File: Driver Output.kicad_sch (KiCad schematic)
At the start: 13 parts, among them U1 DRV8300DRGER

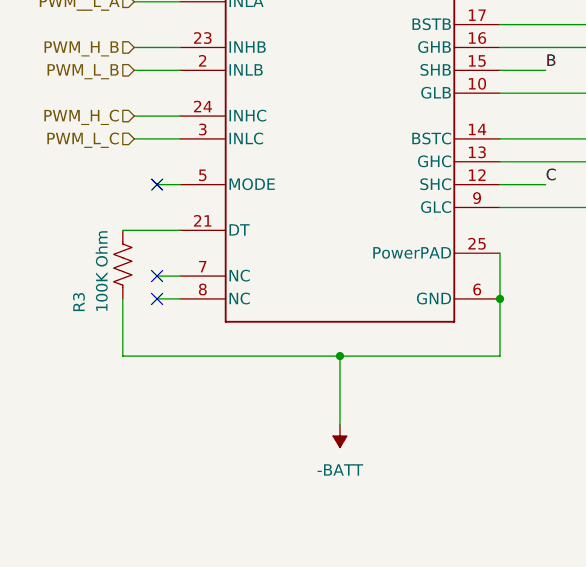
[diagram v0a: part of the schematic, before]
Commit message: Fixed pin names
reset pins to apply proper net names
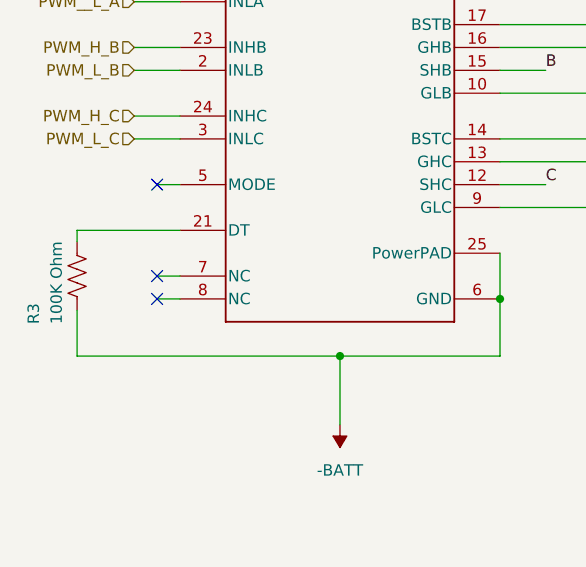
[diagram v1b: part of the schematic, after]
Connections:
- net -BATT: now reaches R10.1, R6.2, R8.1, R9.1
- net -BATT: now also C11.2, R3.2, U1.25 (PowerPAD), U1.6 (GND)
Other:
- moved on the sheet: R3

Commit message: more routing
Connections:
- net Half Bridge - 6S 50A - 2/BST_X renamed BSTB
- net Half Bridge - 6S 50A - 2/GATE_HIGH_X renamed GHB
- net Half Bridge - 6S 50A - 2/GATE_LOW_X renamed GLB
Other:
- sheet Half Bridge - 6S 50A - 1 ports: added X; removed none
- sheet Half Bridge - 6S 50A - 2 ports: added X; removed none
- sheet Half Bridge - 6S 50A - 3 ports: added X; removed none
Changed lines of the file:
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@@
 	(wire
 		(pts
-			(xy 83.82 90.17) (xy 95.25 90.17)
-		)
-		(stroke
-			(width 0)
-			(type default)
-		)
-	)
-	(wire
-		(pts
-			(xy 83.82 74.93) (xy 88.9 74.93)
+			(xy 83.82 90.17) (xy 135.89 90.17)
+		)
+		(stroke
+			(width 0)
+			(type default)
+		)
+	)
+	(wire
+		(pts
+			(xy 83.82 74.93) (xy 97.79 74.93)
 		)
 		(stroke
@@
 	(wire
 		(pts
+			(xy 83.82 59.69) (xy 135.89 59.69)
+		)
+		(stroke
+			(width 0)
+			(type default)
+		)
+	)
+	(wire
+		(pts
 			(xy 66.04 177.8) (xy 66.04 180.34)
 		)
@@
 	(wire
 		(pts
-			(xy 83.82 87.63) (xy 88.9 87.63)
-		)
-		(stroke
-			(width 0)
-			(type default)
-		)
-	)
-	(wire
-		(pts
-			(xy 95.25 62.23) (xy 97.79 62.23)
+			(xy 83.82 87.63) (xy 135.89 87.63)
 		)
 		(stroke
@@
 	(wire
 		(pts
-			(xy 96.52 74.93) (xy 97.79 74.93)
-		)
-		(stroke
-			(width 0)
-			(type default)
-		)
-	)
-	(wire
-		(pts
 			(xy 41.91 57.15) (xy 48.26 57.15)
 		)
@@
 	(wire
 		(pts
-			(xy 83.82 64.77) (xy 95.25 64.77)
+			(xy 83.82 64.77) (xy 135.89 64.77)
 		)
 		(stroke
@@
 	(wire
 		(pts
+			(xy 83.82 57.15) (xy 135.89 57.15)
+		)
+		(stroke
+			(width 0)
+			(type default)
+		)
+	)
+	(wire
+		(pts
 			(xy 60.96 152.4) (xy 80.01 152.4)
 		)
@@
 	(wire
 		(pts
-			(xy 96.52 77.47) (xy 96.52 74.93)
-		)
-		(stroke
-			(width 0)
-			(type default)
-		)
-	)
-	(wire
-		(pts
-			(xy 83.82 59.69) (xy 97.79 59.69)
-		)
-		(stroke
-			(width 0)
-			(type default)
-		)
-	)
-	(wire
-		(pts
 			(xy 50.8 163.83) (xy 55.88 163.83)
 		)
@@
 	(wire
 		(pts
-			(xy 83.82 85.09) (xy 97.79 85.09)
-		)
-		(stroke
-			(width 0)
-			(type default)
-		)
-	)
-	(wire
-		(pts
-			(xy 95.25 64.77) (xy 95.25 62.23)
-		)
-		(stroke
-			(width 0)
-			(type default)
-		)
-	)
-	(wire
-		(pts
-			(xy 83.82 62.23) (xy 88.9 62.23)
-		)
-		(stroke
-			(width 0)
-			(type default)
-		)
-	)
-	(wire
-		(pts
-			(xy 83.82 77.47) (xy 96.52 77.47)
+			(xy 83.82 85.09) (xy 135.89 85.09)
+		)
+		(stroke
+			(width 0)
+			(type default)
+		)
+	)
+	(wire
+		(pts
+			(xy 83.82 62.23) (xy 135.89 62.23)
+		)
+		(stroke
+			(width 0)
+			(type default)
+		)
+	)
+	(wire
+		(pts
+			(xy 83.82 77.47) (xy 97.79 77.47)
 		)
 		(stroke
@@
 	(wire
 		(pts
-			(xy 83.82 57.15) (xy 97.79 57.15)
-		)
-		(stroke
-			(width 0)
-			(type default)
-		)
-	)
-	(wire
-		(pts
 			(xy 36.83 101.6) (xy 36.83 106.68)
 		)
@@
 	(wire
 		(pts
-			(xy 95.25 87.63) (xy 97.79 87.63)
-		)
-		(stroke
-			(width 0)
-			(type default)
-		)
-	)
-	(wire
-		(pts
 			(xy 60.96 162.56) (xy 60.96 163.83)
 		)
@@
 	(wire
 		(pts
-			(xy 95.25 90.17) (xy 95.25 87.63)
-		)
-		(stroke
-			(width 0)
-			(type default)
-		)
-	)
-	(wire
-		(pts
-			(xy 83.82 82.55) (xy 97.79 82.55)
+			(xy 83.82 82.55) (xy 135.89 82.55)
 		)
 		(stroke
@@
 		)
 	)
+	(label "GHB"
+		(at 88.9 72.39 0)
+		(effects
+			(font
+				(size 1.27 1.27)
+			)
+			(justify left bottom)
+		)
+	)
+	(label "BSTB"
+		(at 88.9 69.85 0)
+		(effects
+			(font
+				(size 1.27 1.27)
+			)
+			(justify left bottom)
+		)
+	)
 	(label "A"
 		(at 88.9 62.23 180)
@@
 		)
 	)
+	(label "GLB"
+		(at 88.9 77.47 0)
+		(effects
+			(font
+				(size 1.27 1.27)
+			)
+			(justify left bottom)
+		)
+	)
+	(label "C"
+		(at 88.9 87.63 0)
+		(effects
+			(font
+				(size 1.27 1.27)
+			)
+			(justify left bottom)
+		)
+	)
 	(label "B"
 		(at 99.06 147.32 180)
@@
 			)
 			(justify right bottom)
-		)
-	)
-	(label "C"
-		(at 88.9 87.63 0)
-		(effects
-			(font
-				(size 1.27 1.27)
-			)
-			(justify left bottom)
 		)
 	)
@@
 	)
 	(sheet
-		(at 97.79 55.88)
-		(size 17.78 7.62)
+		(at 135.89 55.88)
+		(size 17.78 10.16)
 		(fields_autoplaced yes)
 		(stroke
@@
 		)
 		(property "Sheetname" "Half Bridge - 6S 50A - 1"
-			(at 97.79 55.1684 0)
+			(at 135.89 55.1684 0)
 			(effects
 				(font
@@
 		)
 		(property "Sheetfile" "Half Bridge - 6S 50A.kicad_sch"
-			(at 97.79 64.0846 0)
+			(at 135.89 66.6246 0)
 			(effects
 				(font
@@
 		)
 		(pin "BST_X" input
-			(at 97.79 57.15 180)
+			(at 135.89 57.15 180)
 			(effects
 				(font
@@
 		)
 		(pin "GATE_LOW_X" input
-			(at 97.79 62.23 180)
+			(at 135.89 64.77 180)
 			(effects
 				(font
@@
 		)
 		(pin "GATE_HIGH_X" input
-			(at 97.79 59.69 180)
+			(at 135.89 59.69 180)
+			(effects
+				(font
+					(size 1.27 1.27)
+				)
+				(justify left)
+			)
+		)
+		(pin "X" input
+			(at 135.89 62.23 180)
 			(effects
 				(font
@@
 	)
 	(sheet
-		(at 97.79 81.28)
-		(size 17.78 7.62)
+		(at 135.89 81.28)
+		(size 17.78 10.16)
 		(fields_autoplaced yes)
 		(stroke
@@
 		)
 		(property "Sheetname" "Half Bridge - 6S 50A - 3"
-			(at 97.79 80.5684 0)
+			(at 135.89 80.5684 0)
 			(effects
 				(font
@@
 		)
 		(property "Sheetfile" "Half Bridge - 6S 50A.kicad_sch"
-			(at 97.79 89.4846 0)
+			(at 135.89 92.0246 0)
 			(effects
 				(font
@@
 		)
 		(pin "BST_X" input
-			(at 97.79 82.55 180)
+			(at 135.89 82.55 180)
 			(effects
 				(font
@@
 		)
 		(pin "GATE_LOW_X" input
-			(at 97.79 87.63 180)
+			(at 135.89 90.17 180)
 			(effects
 				(font
@@
 		)
 		(pin "GATE_HIGH_X" input
-			(at 97.79 85.09 180)
+			(at 135.89 85.09 180)
+			(effects
+				(font
+					(size 1.27 1.27)
+				)
+				(justify left)
+			)
+		)
+		(pin "X" input
+			(at 135.89 87.63 180)
 			(effects
 				(font
@@
 	(sheet
 		(at 97.79 68.58)
-		(size 17.78 7.62)
+		(size 17.78 10.16)
 		(fields_autoplaced yes)
 		(stroke
@@
 		)
 		(property "Sheetfile" "Half Bridge - 6S 50A.kicad_sch"
-			(at 97.79 76.7846 0)
+			(at 97.79 79.3246 0)
 			(effects
 				(font
@@
 		)
 		(pin "GATE_LOW_X" input
-			(at 97.79 74.93 180)
+			(at 97.79 77.47 180)
 			(effects
 				(font
@@
 			(effects
 				(font
+					(size 1.27 1.27)
+				)
+				(justify left)
+			)
+		)
+		(pin "X" input
+			(at 97.79 74.93 180)
+			(effects
+				(font

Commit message: more routing and placement
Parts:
- renumbered C11 to C24, U1 to U3
